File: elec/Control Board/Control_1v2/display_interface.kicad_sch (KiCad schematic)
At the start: 4 parts, among them J35 Conn_02x05_Odd_Even, J36 Conn_02x05_Odd_Even

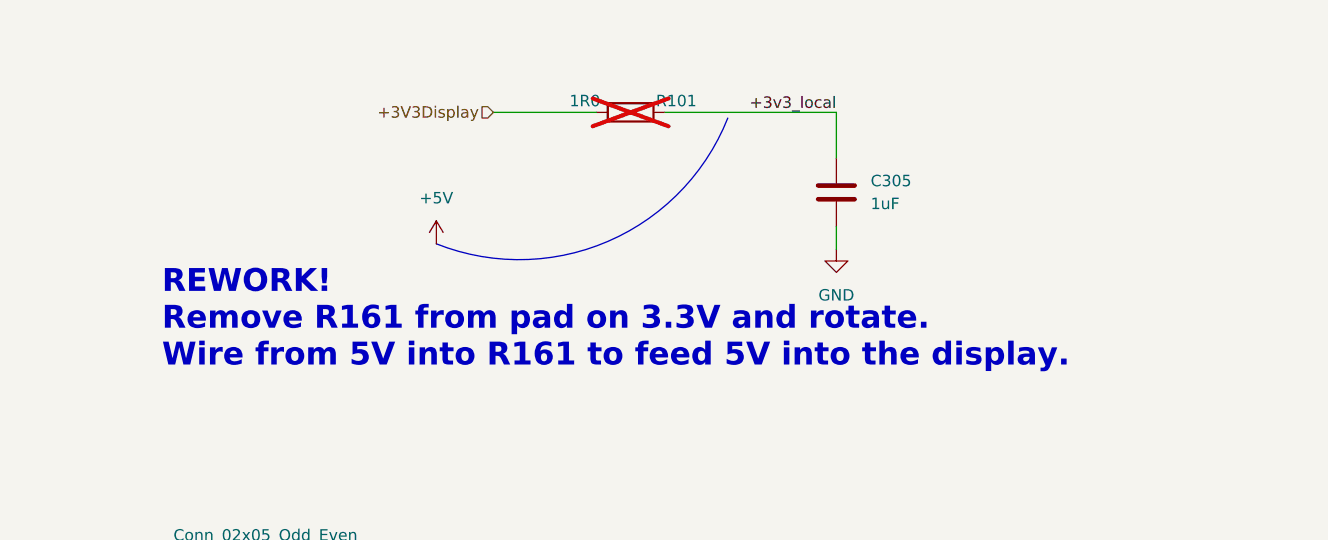
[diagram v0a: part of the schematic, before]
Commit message: Contrl 1.2 schematic Issue Mini-12864-Panel 3.3v on display 2.4ish volts #110
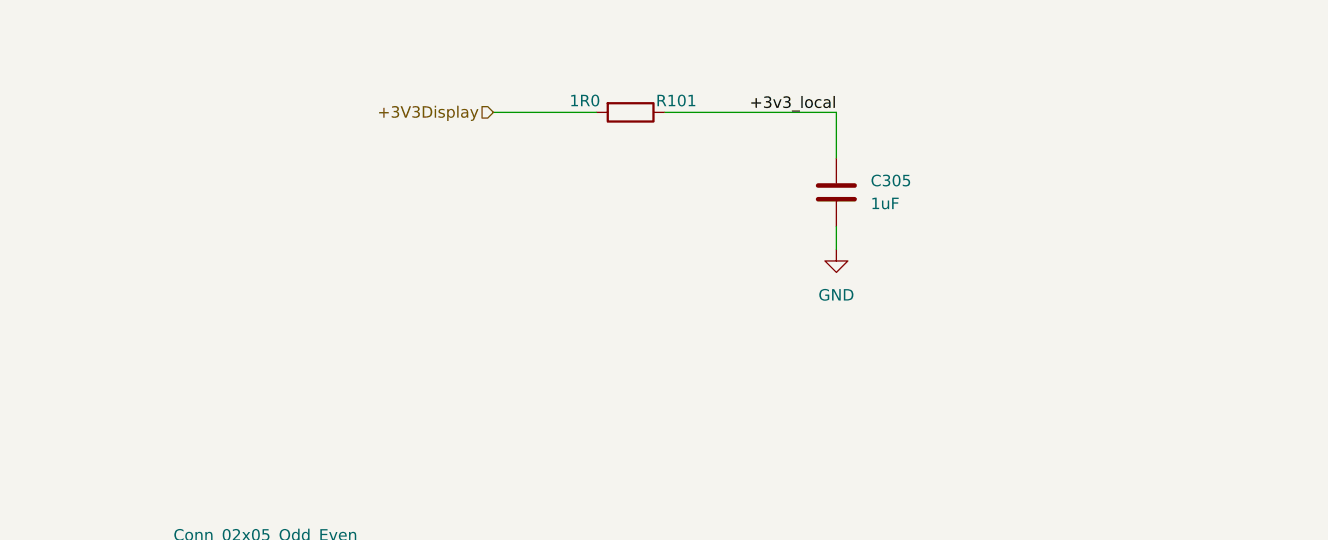
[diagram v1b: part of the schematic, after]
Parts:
- R101: now fitted
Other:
- note removed: "REWORK! Remove R161 from pad on 3.3V and rotate. Wire from 5V into R161 to feed 5V into the display."
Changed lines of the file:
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@@
-    (fill (type none))
-  )
-  (arc (start 231.775 28.575) (mid 218.4758 42.2672) (end 199.39 42.545)
-    (stroke (width 0) (type default))
     (fill (type none))
   )
@@
     (effects (font (size 1.27 1.27)) (justify right bottom))
   )
-  (text "REWORK!\nRemove R161 from pad on 3.3V and rotate. \nWire from 5V into R161 to feed 5V into the display."
-    (at 168.91 56.515 0)
-    (effects (font (size 2.54 2.54) (thickness 0.508) bold) (justify left bottom))
-  )
   (text "ST7920 can not share an SPI/Serial interface)" (at 25.4 166.37 0)
     (effects (font (size 1.27 1.27)) (justify left bottom))
@@
     )
   )
-  (symbol (lib_id "power:+5V") (at 199.39 42.545 0) (unit 1)
-    (in_bom yes) (on_board yes) (dnp no) (fields_autoplaced)
-    (property "Reference" "#PWR025" (at 199.39 46.355 0)
-      (effects (font (size 1.27 1.27)) hide)
-    )
-    (property "Value" "+5V" (at 199.39 37.465 0)
-      (effects (font (size 1.27 1.27)))
-    )
-    (property "Footprint" "" (at 199.39 42.545 0)
-      (effects (font (size 1.27 1.27)) hide)
-    )
-    (property "Datasheet" "" (at 199.39 42.545 0)
-      (effects (font (size 1.27 1.27)) hide)
-    )
-    (pin "1")
-    (instances
-      (project "Control_1v2"
-        (path "/c68c9deb-8d4d-42f0-adf8-4d3022f4ee59"
-          (reference "#PWR025") (unit 1)
-        )
-        (path "/c68c9deb-8d4d-42f0-adf8-4d3022f4ee59/f2cc20dc-f81b-4e9e-a9e1-88ed6ea8264c"
-          (reference "#PWR0108") (unit 1)
-        )
-      )
-    )
-  )
   (symbol (lib_id "Connector_Generic:Conn_02x05_Odd_Even") (at 180.34 85.09 180) (unit 1)
     (in_bom yes) (on_board yes) (dnp no)
@@
   )
   (symbol (lib_id "Device:R") (at 220.98 27.94 270) (unit 1)
-    (in_bom yes) (on_board yes) (dnp yes)
+    (in_bom yes) (on_board yes) (dnp no)
     (property "Reference" "R101" (at 226.06 26.67 90)
       (effects (font (size 1.27 1.27)))

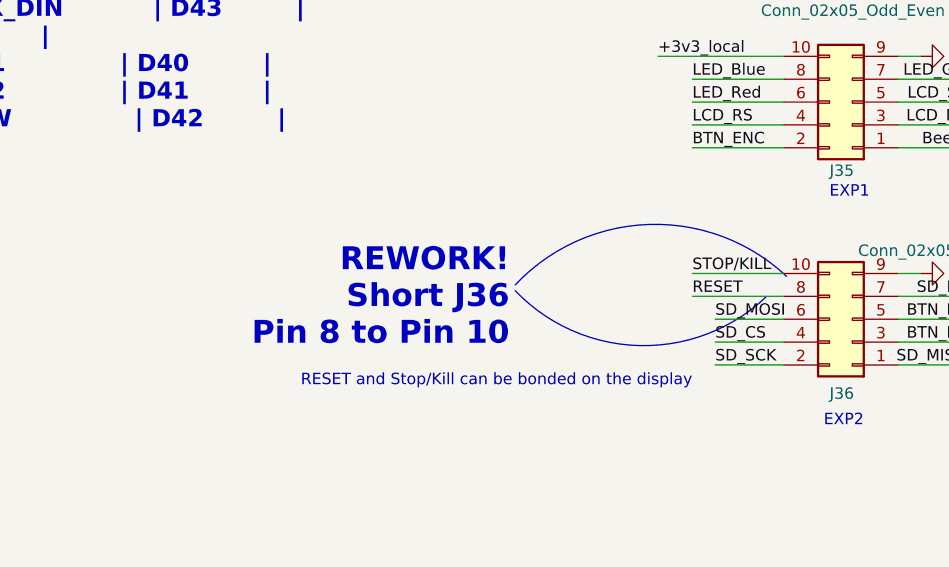
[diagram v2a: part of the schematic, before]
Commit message: Contrl 1.2 schematic, fix for Issue: Mini-12864-Panel STOP/KILL NP on R7, SHUTDOWN button Inoperative #109
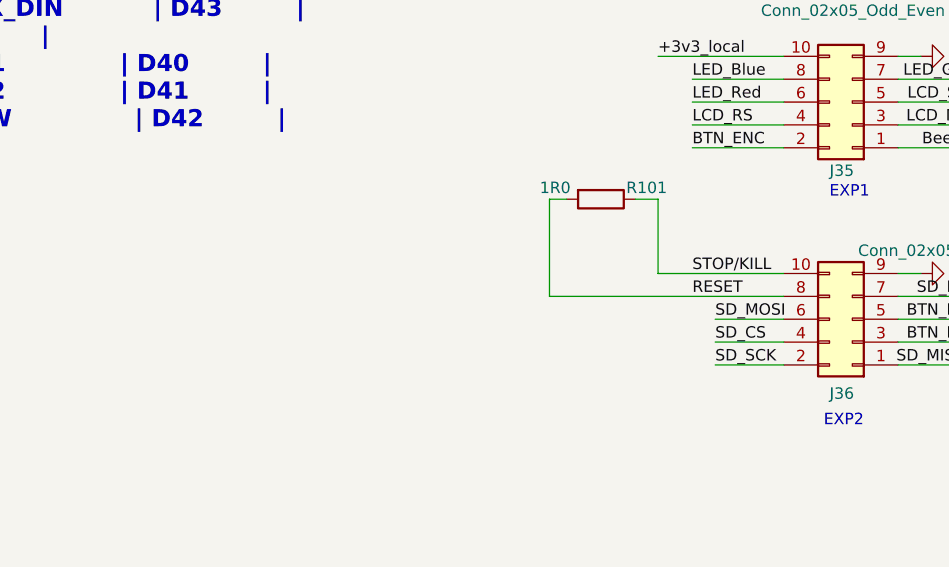
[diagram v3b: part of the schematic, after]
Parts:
- added R101: 1R0, Resistor_SMD:R_0603_1608Metric_Pad0.98x0.95mm_HandSolder, symbol Device:R
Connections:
- net RESET: now also R101.2
- net STOP/KILL: now also R101.1
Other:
- note removed: "RESET and Stop/Kill can be bonded on the display"
- note removed: "REWORK! Short J36 Pin 8 to Pin 10"
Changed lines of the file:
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@@
+    (stroke (width 0) (type default))
+  )
+  (wire (pts (xy 146.685 106.68) (xy 146.685 95.885))
     (stroke (width 0) (type default))
   )
@@
     (stroke (width 0) (type default))
   )
-  (wire (pts (xy 162.56 106.68) (xy 172.72 106.68))
+  (wire (pts (xy 146.685 106.68) (xy 172.72 106.68))
     (stroke (width 0) (type default))
   )
@@
     (stroke (width 0) (type default))
   )
+  (wire (pts (xy 156.21 95.885) (xy 158.75 95.885))
+    (stroke (width 0) (type default))
+  )
   (wire (pts (xy 267.97 102.235) (xy 248.92 102.235))
     (stroke (width 0) (type default))
@@
     (stroke (width 0) (type default))
   )
+  (wire (pts (xy 158.75 95.885) (xy 158.75 104.14))
+    (stroke (width 0) (type default))
+  )
   (wire (pts (xy 165.1 109.22) (xy 172.72 109.22))
     (stroke (width 0) (type default))
@@
     (stroke (width 0) (type default))
   )
+  (wire (pts (xy 146.685 95.885) (xy 148.59 95.885))
+    (stroke (width 0) (type default))
+  )
   (wire (pts (xy 185.42 106.68) (xy 194.31 106.68))
     (stroke (width 0) (type default))
@@
     (stroke (width 0) (type default))
   )
-  (wire (pts (xy 162.56 104.14) (xy 172.72 104.14))
+  (wire (pts (xy 158.75 104.14) (xy 172.72 104.14))
     (stroke (width 0) (type default))
   )
@@
   (wire (pts (xy 165.1 114.3) (xy 172.72 114.3))
     (stroke (width 0) (type default))
-  )
-  (arc (start 170.815 106.68) (mid 156.7133 112.1496) (end 142.875 106.045)
-    (stroke (width 0) (type default))
-    (fill (type none))
-  )
-  (arc (start 142.875 105.41) (mid 157.7588 98.6879) (end 173.037 104.458)
-    (stroke (width 0) (type default))
-    (fill (type none))
   )
   (image (at 217.805 133.35)
@@
     )
   )
-  (text "RESET and Stop/Kill can be bonded on the display" (at 162.56 116.84 0)
-    (effects (font (size 1.27 1.27)) (justify right bottom))
-  )
   (text "EXP2" (at 251.46 78.105 0)
     (effects (font (size 1.27 1.27)) (justify left bottom))
@@
     (at 19.05 88.265 0)
     (effects (font (face "Courier New") (size 1.905 1.905) (thickness 0.381) bold) (justify left bottom))
-  )
-  (text "REWORK!\nShort J36\nPin 8 to Pin 10" (at 142.24 112.395 0)
-    (effects (font (size 2.54 2.54) (thickness 0.508) bold) (justify right bottom))
   )
   (text "EXP1\n" (at 209.55 79.375 0)
@@
         )
       )
+    )
+  )
+  (symbol (lib_id "Device:R") (at 152.4 95.885 270) (unit 1)
+    (in_bom yes) (on_board yes) (dnp no)
+    (property "Reference" "R101" (at 157.48 94.615 90)
+      (effects (font (size 1.27 1.27)))
+    )
+    (property "Value" "1R0" (at 147.32 94.615 90)
+      (effects (font (size 1.27 1.27)))
+    )
+    (property "Footprint" "Resistor_SMD:R_0603_1608Metric_Pad0.98x0.95mm_HandSolder" (at 152.4 94.107 90)
+      (effects (font (size 1.27 1.27)) hide)
+    )
+    (property "Datasheet" "~" (at 152.4 95.885 0)
+      (effects (font (size 1.27 1.27)) hide)
+    )
+    (property "Distributor 1" "JLCPCB" (at 152.4 95.885 90)
+      (effects (font (size 1.27 1.27)) hide)
+    )
+    (property "Distributor 1 PN" "C269434" (at 152.4 95.885 90)
+      (effects (font (size 1.27 1.27)) hide)
+    )
+    (property "Manufacturer" "TyoHM" (at 152.4 95.885 90)
+      (effects (font (size 1.27 1.27)) hide)
+    )
+    (property "MPN" "RMC060315%N" (at 152.4 95.885 90)
+      (effects (font (size 1.27 1.27)) hide)
+    )
+    (property "Description" "0.1W ±5% 1Ω 0603 Chip Resistor - Surface Mount ROHS" (at 152.4 95.885 0)
+      (effects (font (size 1.27 1.27)) hide)
+    )
+    (property "AssemblyType" "SMT" (at 152.4 95.885 0)
+      (effects (font (size 1.27 1.27)) hide)
+    )
+    (property "Cost" "0.0015" (at 152.4 95.885 0)
+      (effects (font (size 1.27 1.27)) hide)
+    )
+    (property "LongLead" "NO" (at 152.4 95.885 0)
+      (effects (font (size 1.27 1.27)) hide)
+    )
+    (pin "1")
+    (pin "2")
+    (instances
+      (project "GeneralPurposeAlarmDevicePCB"
+        (path "/412a327d-1ee3-473e-bc00-1545004b7edf"
+          (reference "R101") (unit 1)
+        )
+      )
+      (project "Control_1v2"
+        (path "/c68c9deb-8d4d-42f0-adf8-4d3022f4ee59/0cb2f0dc-fe38-451d-b752-5d12a98f8d03"
+          (reference "R9") (unit 1)
+        )
+        (path "/c68c9deb-8d4d-42f0-adf8-4d3022f4ee59"
+          (reference "R144") (unit 1)
+        )
+        (path "/c68c9deb-8d4d-42f0-adf8-4d3022f4ee59/3ff32a52-b1ed-4756-8661-90a95f721605"
+          (reference "R7") (unit 1)
+        )
+        (path "/c68c9deb-8d4d-42f0-adf8-4d3022f4ee59/3daed20d-8623-449a-af6f-871db7628ab2"
+          (reference "R20") (unit 1)
+        )
+        (path "/c68c9deb-8d4d-42f0-adf8-4d3022f4ee59/f2cc20dc-f81b-4e9e-a9e1-88ed6ea8264c"
+          (reference "R?") (unit 1)
+        )
+      )

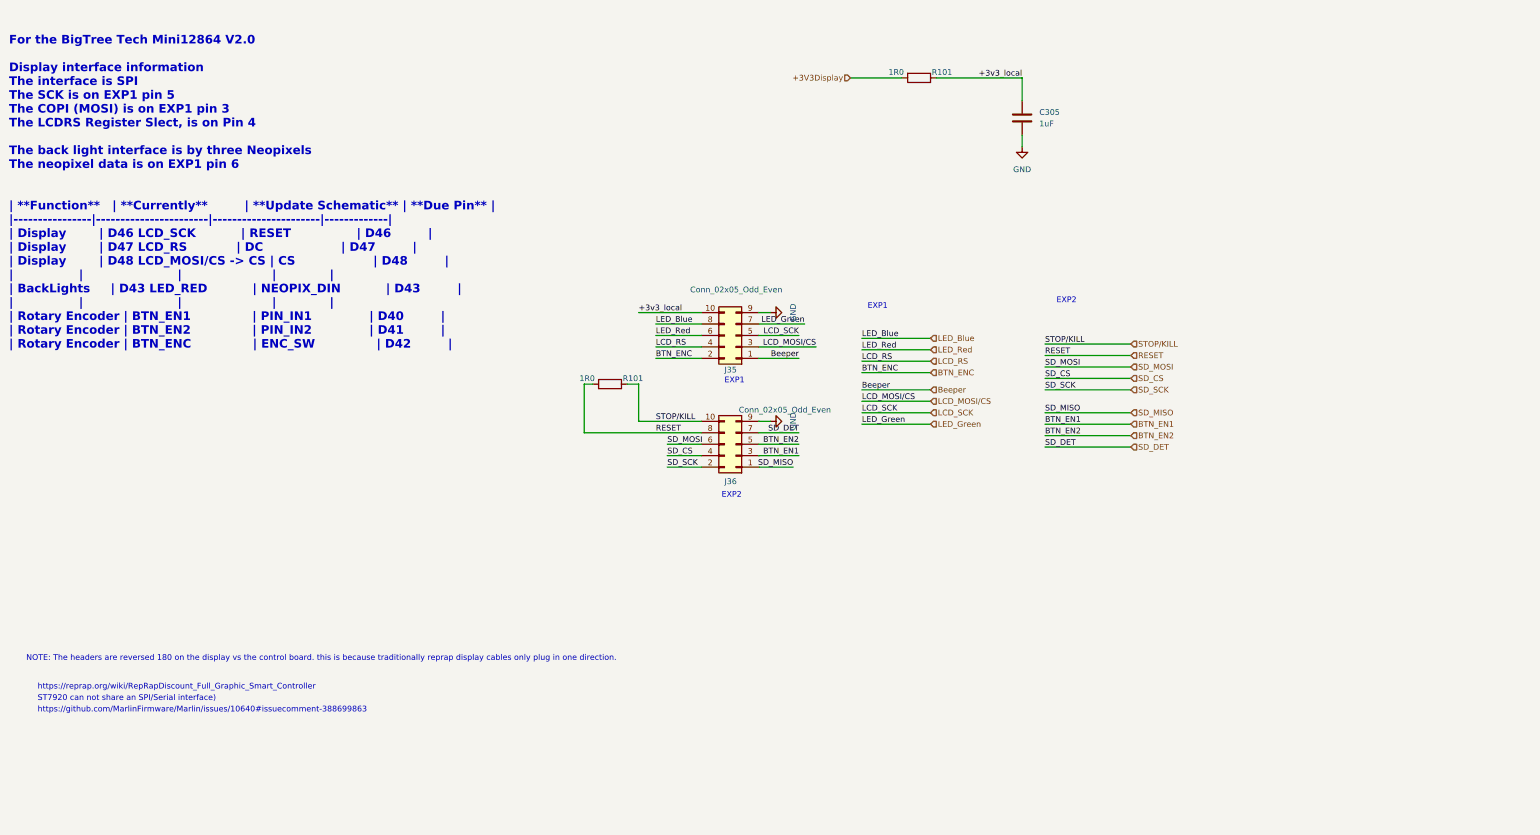
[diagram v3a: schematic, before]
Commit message: Contrl 1.2 schematic, adding relay for the battery. Adding connector for Status and Fault front panel LEDs.
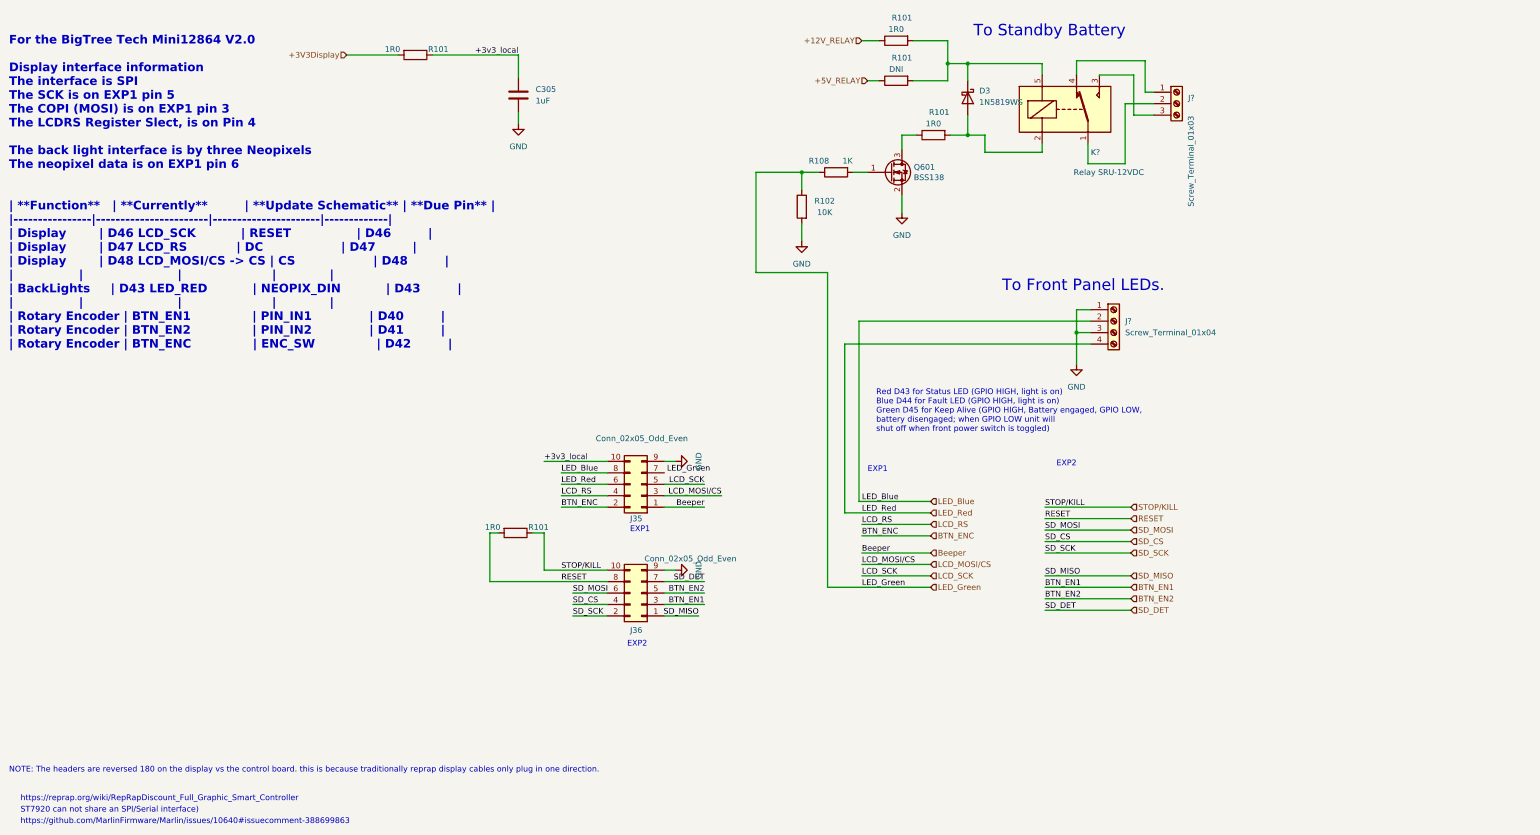
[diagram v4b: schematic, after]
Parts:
- added D3: 1N5819WS, Diode_SMD:D_SOD-323, symbol Diode:1N5819WS
- added J?: Screw_Terminal_01x04, TerminalBlock_TE-Connectivity:TerminalBlock_TE_282834-4_1x04_P2.54mm_Horizontal, symbol Connector:Screw_Terminal_01x04
- added J?: Screw_Terminal_01x03, TerminalBlock_TE-Connectivity:TerminalBlock_TE_282834-3_1x03_P2.54mm_Horizontal, symbol Connector:Screw_Terminal_01x03
- added K?: Relay SRU-12VDC, Relay_THT:Relay_SPDT_Omron-G5LE-1, symbol Relay:G5LE-1
- added Q601: BSS138, Package_TO_SOT_SMD:SOT-23, symbol Transistor_FET:BSS138
- added R101 (x2): 1R0, Resistor_SMD:R_0603_1608Metric_Pad0.98x0.95mm_HandSolder, symbol Device:R
- added R101: DNI, Resistor_SMD:R_0603_1608Metric_Pad0.98x0.95mm_HandSolder, symbol Device:R
- added R102: 10K, Resistor_SMD:R_0603_1608Metric_Pad0.98x0.95mm_HandSolder, symbol Device:R
- added R108: 1K, Resistor_SMD:R_0603_1608Metric_Pad0.98x0.95mm_HandSolder, symbol Device:R
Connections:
- net GND: now also J?.1 (Pin_1), J?.3 (Pin_3), Q601.2 (S), R102.2
- net LED_Blue: now also J?.2 (Pin_2)
- net LED_Green: now also R102.1, R108.1; no longer J35.7 (Pin_7)
- net LED_Red: now also J?.4 (Pin_4)
- new net: Q601.3 (D), R101.1
- new net: D3.2 (A), K?.2, R101.2
- new net: J?.2 (Pin_2), K?.1
- new net: J?.3 (Pin_3), K?.3
- new net: J?.1 (Pin_1), K?.4
- new net: D3.1 (K), K?.5, R101.2, R101.2
- new net: Q601.1 (G), R108.2
- new net +12V_RELAY: R101.1
- new net +5V_RELAY: R101.1
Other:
- note added: "Red D43 for Status LED (GPIO HIGH, light is on) Blue D44 for Fault LED (GPIO HIGH, light is on) Green D45 for Keep Alive (GPIO HIGH, Battery engaged, GPIO LOW, battery disengaged; when GPIO LOW unit will shut off when front power switch is toggled)"
- note added: "To Front Panel LEDs."
- note added: "To Standby Battery"
- moved on the sheet: C305, J35, J36, R101
